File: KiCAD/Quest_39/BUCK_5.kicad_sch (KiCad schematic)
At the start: 32 parts, among them U24 AD626ANZ, U25 INA226, U26 LTM4611EV-PBF, U27 MCP4151-502E/SN

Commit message: Fixed INA226 schem. mistake and further layout work
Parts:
- added C93: 100nF, Capacitor_SMD:C_0603_1608Metric, symbol Device:C
- renumbered C94 to C100, C95 to C101, C96 to C102, C97 to C103, C84 to C89, C85 to C90, C86 to C91, C87 to C92, C88 to C94, C89 to C95, C90 to C96, C91 to C97, C92 to C98, C93 to C99
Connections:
- net +5V: now also C93.1
- net GND: now also C93.2
- net PV_POS: no longer C89.1, C90.1, C91.1, C92.1, R52.2, R54.1, R57.1, U26.A1 (VIN), U26.A2 (VIN), U26.A3 (VIN), U26.A4 (VIN), U26.A5 (VIN), U26.A6 (VIN), U26.B1 (VIN), U26.B2 (VIN), U26.B3 (VIN), U26.B4 (VIN), U26.B5 (VIN), U26.B6 (VIN), U26.C1 (VIN), U26.C2 (VIN), U26.C3 (VIN), U26.C4 (VIN), U26.C5 (VIN), U26.C6 (VIN)
- net Vin-: no longer TP42.1, U24.5 (OUT), U25.8 (Vbus)
- new net: TP42.1, U24.5 (OUT), U25.8 (Vbus)
- new net BUCK_VIN: C89.1, C90.1, C91.1, C92.1, R52.2, R54.1, R57.1, U26.A1 (VIN), U26.A2 (VIN), U26.A3 (VIN), U26.A4 (VIN), U26.A5 (VIN), U26.A6 (VIN), U26.B1 (VIN), U26.B2 (VIN), U26.B3 (VIN), U26.B4 (VIN), U26.B5 (VIN), U26.B6 (VIN), U26.C1 (VIN), U26.C2 (VIN), U26.C3 (VIN), U26.C4 (VIN), U26.C5 (VIN), U26.C6 (VIN)

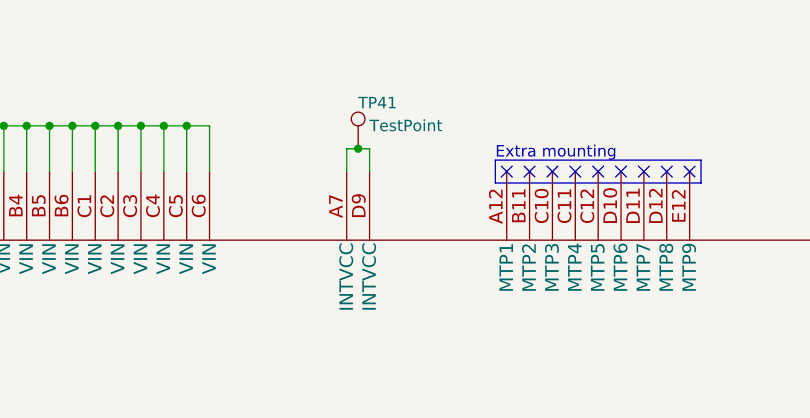
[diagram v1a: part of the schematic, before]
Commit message: Partial wiring of first buck converter section PCB layout
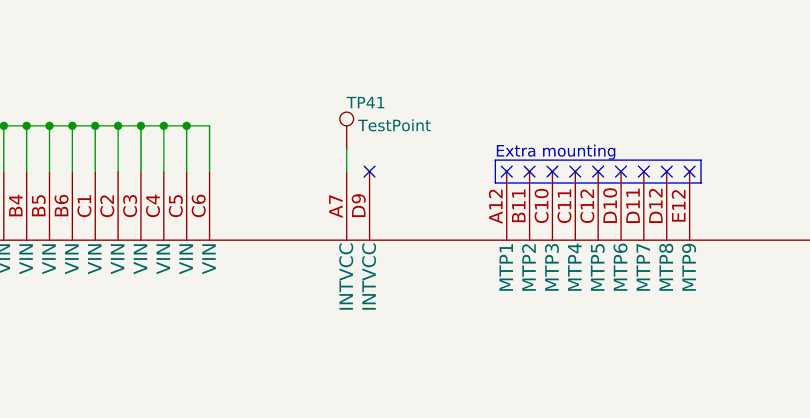
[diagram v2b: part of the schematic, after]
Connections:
- net at TP41.1, U26.A7 (INTVCC): no longer U26.D9 (INTVCC)
- no-connect marks 12 -> 13
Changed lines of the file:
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@@
   (junction (at 322.58 99.06) (diameter 0) (color 0 0 0 0)
   )
-  (junction (at 234.95 38.1) (diameter 0) (color 0 0 0 0)
-  )
   (junction (at 185.42 200.66) (diameter 0) (color 0 0 0 0)
   )
@@
   )
   (no_connect (at 271.78 40.64))
+  (no_connect (at 236.22 40.64))
   (no_connect (at 251.46 40.64))
   (no_connect (at 269.24 40.64))
@@
     (stroke (width 0) (type default) (color 0 0 0 0))
   )
-  (wire (pts (xy 233.68 38.1) (xy 234.95 38.1))
-    (stroke (width 0) (type default) (color 0 0 0 0))
-  )
   (wire (pts (xy 167.64 200.66) (xy 165.1 200.66))
     (stroke (width 0) (type default) (color 0 0 0 0))
@@
     (stroke (width 0) (type default) (color 0 0 0 0))
   )
-  (wire (pts (xy 236.22 38.1) (xy 236.22 40.64))
-    (stroke (width 0) (type default) (color 0 0 0 0))
-  )
-  (wire (pts (xy 234.95 38.1) (xy 236.22 38.1))
-    (stroke (width 0) (type default) (color 0 0 0 0))
-  )
   (wire (pts (xy 193.04 35.56) (xy 193.04 40.64))
     (stroke (width 0) (type default) (color 0 0 0 0))
@@
     (stroke (width 0) (type default) (color 0 0 0 0))
   )
+  (wire (pts (xy 233.68 40.64) (xy 233.68 38.1))
+    (stroke (width 0) (type default) (color 0 0 0 0))
+  )
   (wire (pts (xy 105.41 72.39) (xy 105.41 66.04))
     (stroke (width 0) (type default) (color 0 0 0 0))
@@
   )
   (wire (pts (xy 107.95 64.77) (xy 107.95 66.04))
-    (stroke (width 0) (type default) (color 0 0 0 0))
-  )
-  (wire (pts (xy 233.68 40.64) (xy 233.68 38.1))
     (stroke (width 0) (type default) (color 0 0 0 0))
   )
@@
     (pin "2")
   )
-  (symbol (lib_id "Connector:TestPoint") (at 234.95 38.1 0) (unit 1)
-    (in_bom yes) (on_board yes)
-    (property "Reference" "TP41" (id 0) (at 234.95 33.02 0)
-      (effects (font (size 1.27 1.27)) (justify left))
-    )
-    (property "Value" "TestPoint" (id 1) (at 236.22 35.56 0)
-      (effects (font (size 1.27 1.27)) (justify left))
-    )
-    (property "Footprint" "TestPoint:TestPoint_Pad_D2.0mm" (id 2) (at 240.03 38.1 0)
-      (effects (font (size 1.27 1.27)) hide)
-    )
-    (property "Datasheet" "~" (id 3) (at 240.03 38.1 0)
-      (effects (font (size 1.27 1.27)) hide)
-    )
-    (pin "1")
-  )
   (symbol (lib_id "Device:C") (at 356.87 163.83 0) (unit 1)
     (in_bom yes) (on_board yes)
@@
     (pin "2")
   )
+  (symbol (lib_id "Connector:TestPoint") (at 233.68 38.1 0) (unit 1)
+    (in_bom yes) (on_board yes)
+    (property "Reference" "TP41" (id 0) (at 233.68 33.02 0)
+      (effects (font (size 1.27 1.27)) (justify left))
+    )
+    (property "Value" "TestPoint" (id 1) (at 234.95 35.56 0)
+      (effects (font (size 1.27 1.27)) (justify left))
+    )
+    (property "Footprint" "TestPoint:TestPoint_Pad_D2.0mm" (id 2) (at 238.76 38.1 0)
+      (effects (font (size 1.27 1.27)) hide)
+    )
+    (property "Datasheet" "~" (id 3) (at 238.76 38.1 0)
+      (effects (font (size 1.27 1.27)) hide)
+    )
+    (pin "1")
+  )
   (symbol (lib_id "Device:R") (at 25.4 59.69 0) (unit 1)

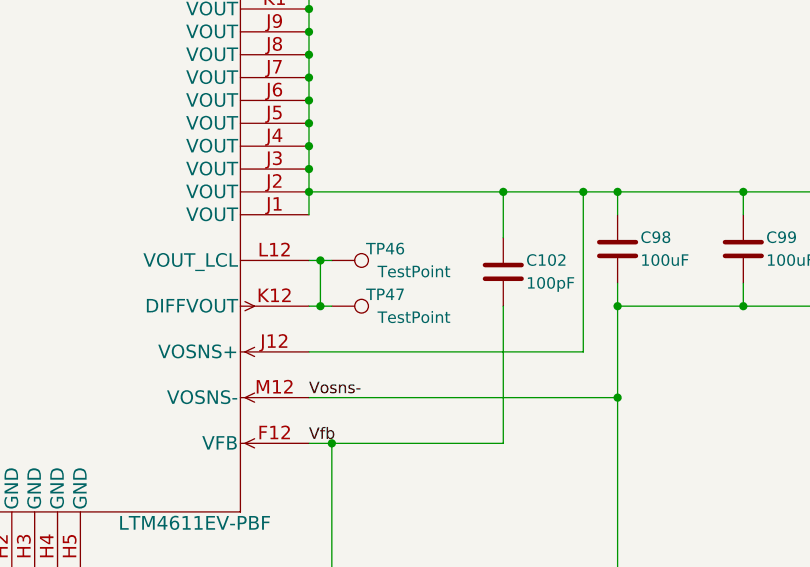
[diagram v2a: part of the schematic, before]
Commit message: Added 3rd buck converter section
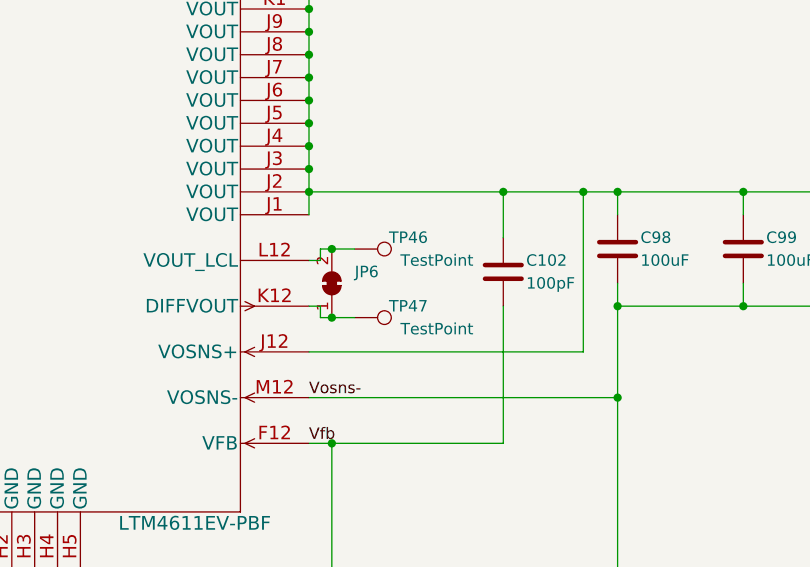
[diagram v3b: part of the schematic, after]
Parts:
- added JP6: SolderJumper_2_Bridged, Jumper:SolderJumper-2_P1.3mm_Bridged_RoundedPad1.0x1.5mm, symbol Jumper:SolderJumper_2_Bridged
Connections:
- net at TP47.1, U26.K12 (DIFFVOUT): now also JP6.1 (A); no longer TP46.1, U26.L12 (VOUT_LCL)
- new net: JP6.2 (B), TP46.1, U26.L12 (VOUT_LCL)
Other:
- moved on the sheet: TP46, TP47

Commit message: Added all the SolidWorks files, edited README
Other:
- title: (none) -> BUCK_5
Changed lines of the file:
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@@
 (kicad_sch (version 20211123) (generator eeschema)
   (paper "A3")
+  (title_block
+    (title "BUCK_5")
+    (date "2023-01-31")
+    (rev "1.0")
+  )
   (junction (at 383.54 157.48) (diameter 0) (color 0 0 0 0)
   )
